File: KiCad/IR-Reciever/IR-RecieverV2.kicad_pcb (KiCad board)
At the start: 2 copper layers, 19.7 x 17.8 mm, 6 parts, among them P1 CONN_6, U1 TSOP38238, U2 TSOP38238, U3 TSOP38238, U4 RGBLED

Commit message: Revert "Revert "3/29 KiCad Updates""
This reverts commit 46467126b97e8d3ee2ff82587e11af580e6d6854.
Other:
- board text added: "Apparel Sensor Array v1"
- board text removed: "Apparel Sensor Array"
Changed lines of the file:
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@@
     )
   )
-  (gr_text "Apparel Sensor Array" (at 45.974 22.86) (layer F.SilkS)
+  (gr_text "Apparel Sensor Array v1" (at 45.974 22.86) (layer F.SilkS)
     (effects (font (size 0.5 0.5) (thickness 0.125)) (justify right))
   )

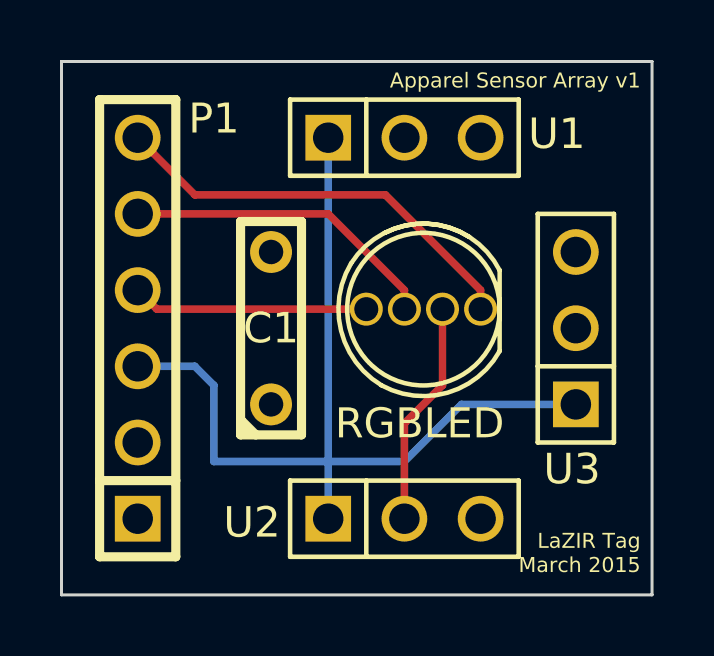
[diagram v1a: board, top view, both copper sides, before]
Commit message: Revert "3/29 KiCad Updates"
This reverts commit a2529da1b40b1f6e0e832ed1976ed3be41434859.
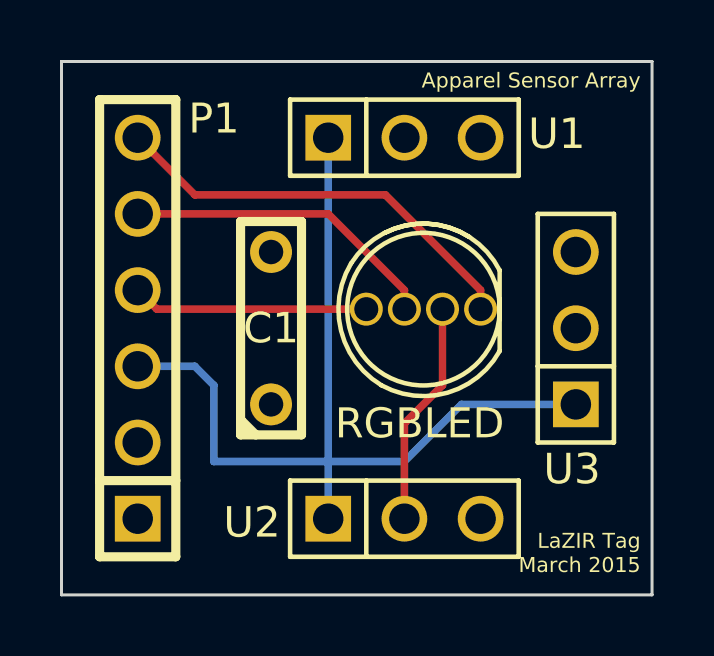
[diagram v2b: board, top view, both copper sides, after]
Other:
- board text added: "Apparel Sensor Array"
- board text removed: "Apparel Sensor Array v1"
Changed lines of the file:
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@@
     )
   )
-  (gr_text "Apparel Sensor Array v1" (at 45.974 22.86) (layer F.SilkS)
+  (gr_text "Apparel Sensor Array" (at 45.974 22.86) (layer F.SilkS)
     (effects (font (size 0.5 0.5) (thickness 0.125)) (justify right))
   )
